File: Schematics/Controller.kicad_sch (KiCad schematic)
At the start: 25 parts, among them IC1 F280049CPMSR, J15 43650-0418, J19 FTSH-105-01-LM-D-K, J20 43650-0418, J22 43045-1212, Y1 ABM8-20.000MHZ-B2-T

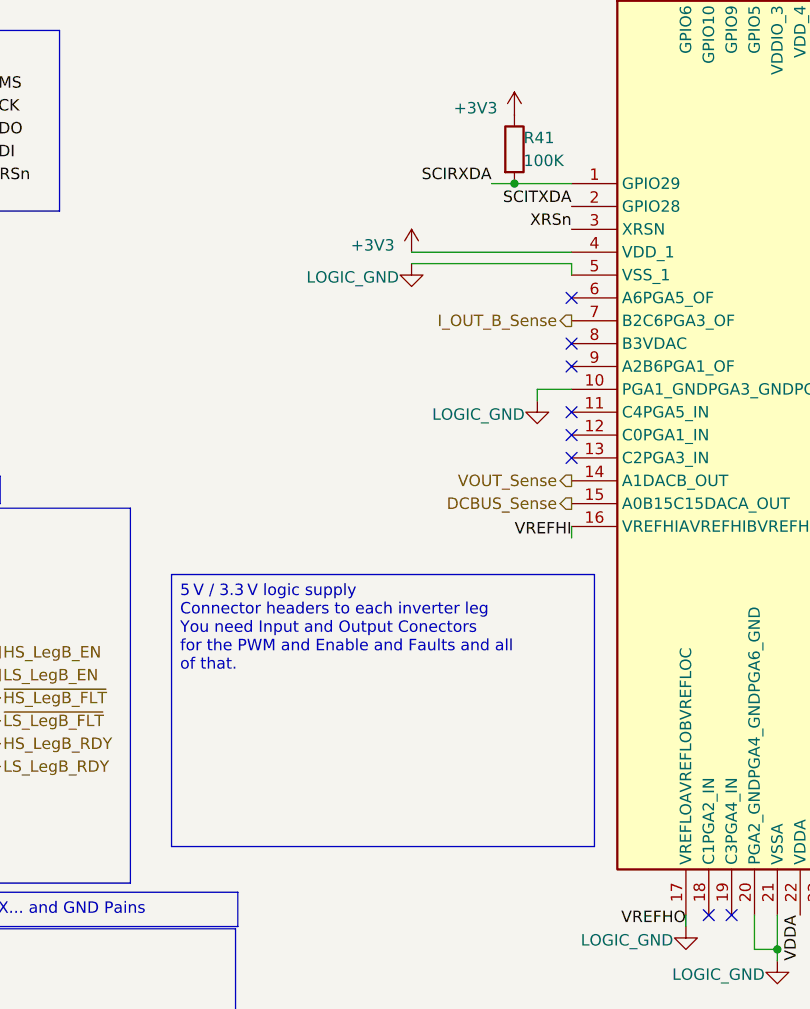
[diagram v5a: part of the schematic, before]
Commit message: [WIP Controller Subsheet]
- Added USB sub sheet to allow use of a USB connection to controller
- Added USB parts for USB Circuit
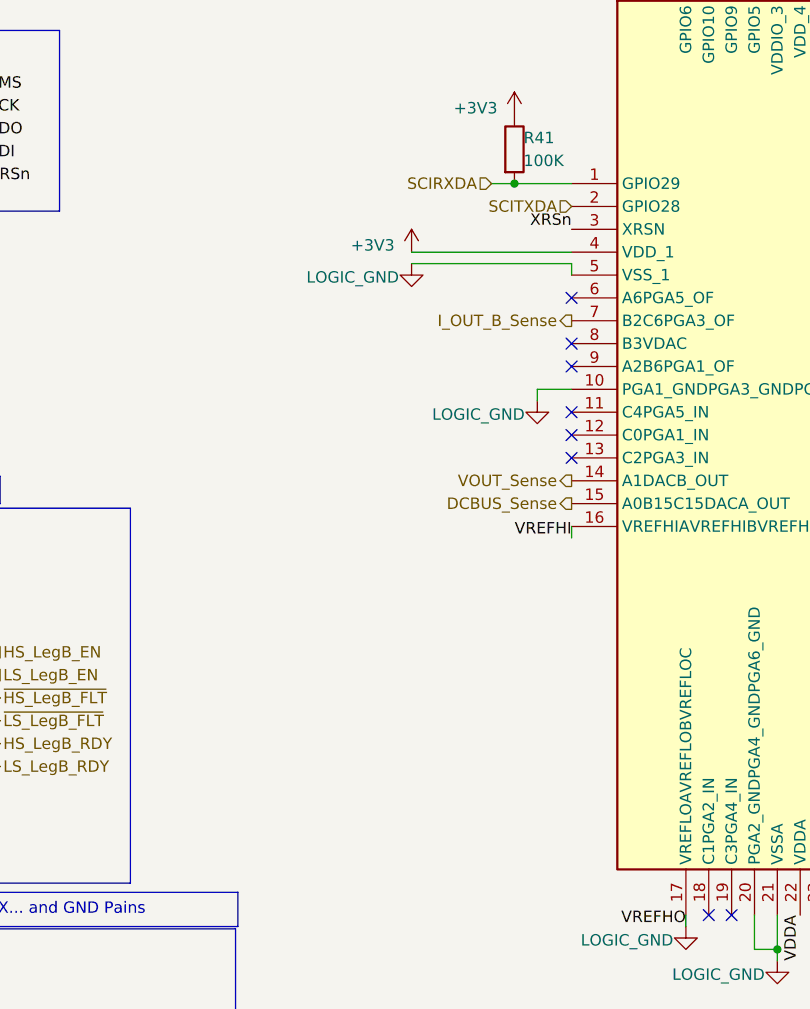
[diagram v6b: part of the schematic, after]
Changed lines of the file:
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@@
-		)
-	)
-	(text_box "5 V / 3.3 V logic supply\nConnector headers to each inverter leg\nYou need Input and Output Conectors \nfor the PWM and Enable and Faults and all of that. "
-		(exclude_from_sim no)
-		(at 73.66 108.204 0)
-		(size 46.99 30.226)
-		(margins 0.9525 0.9525 0.9525 0.9525)
-		(stroke
-			(width 0)
-			(type solid)
-		)
-		(fill
-			(type color)
-			(color 0 0 255 0.1)
-		)
-		(effects
-			(font
-				(size 1.27 1.27)
-			)
-			(justify left top)
 		)
 	)
@@
 		)
 	)
-	(label "SCITXDA"
-		(at 118.11 67.31 180)
-		(effects
-			(font
-				(size 1.27 1.27)
-			)
-			(justify right bottom)
-		)
-	)
 	(label "TCK"
 		(at 270.51 21.59 0)
@@
 			)
 			(justify left bottom)
-		)
-	)
-	(label "SCIRXDA"
-		(at 109.22 64.77 180)
-		(effects
-			(font
-				(size 1.27 1.27)
-			)
-			(justify right bottom)
 		)
 	)
@@
 		)
 	)
+	(hierarchical_label "SCIRXDA"
+		(shape input)
+		(at 109.22 64.77 180)
+		(effects
+			(font
+				(size 1.27 1.27)
+			)
+			(justify right)
+		)
+	)
 	(hierarchical_label "ePWM_A_H"
 		(shape input)
@@
 		(effects
 			(font
+				(size 1.27 1.27)
+			)
+			(justify right)
+		)
+	)
+	(hierarchical_label "SCITXDA"
+		(shape input)
+		(at 118.11 67.31 180)
+		(effects
+			(font

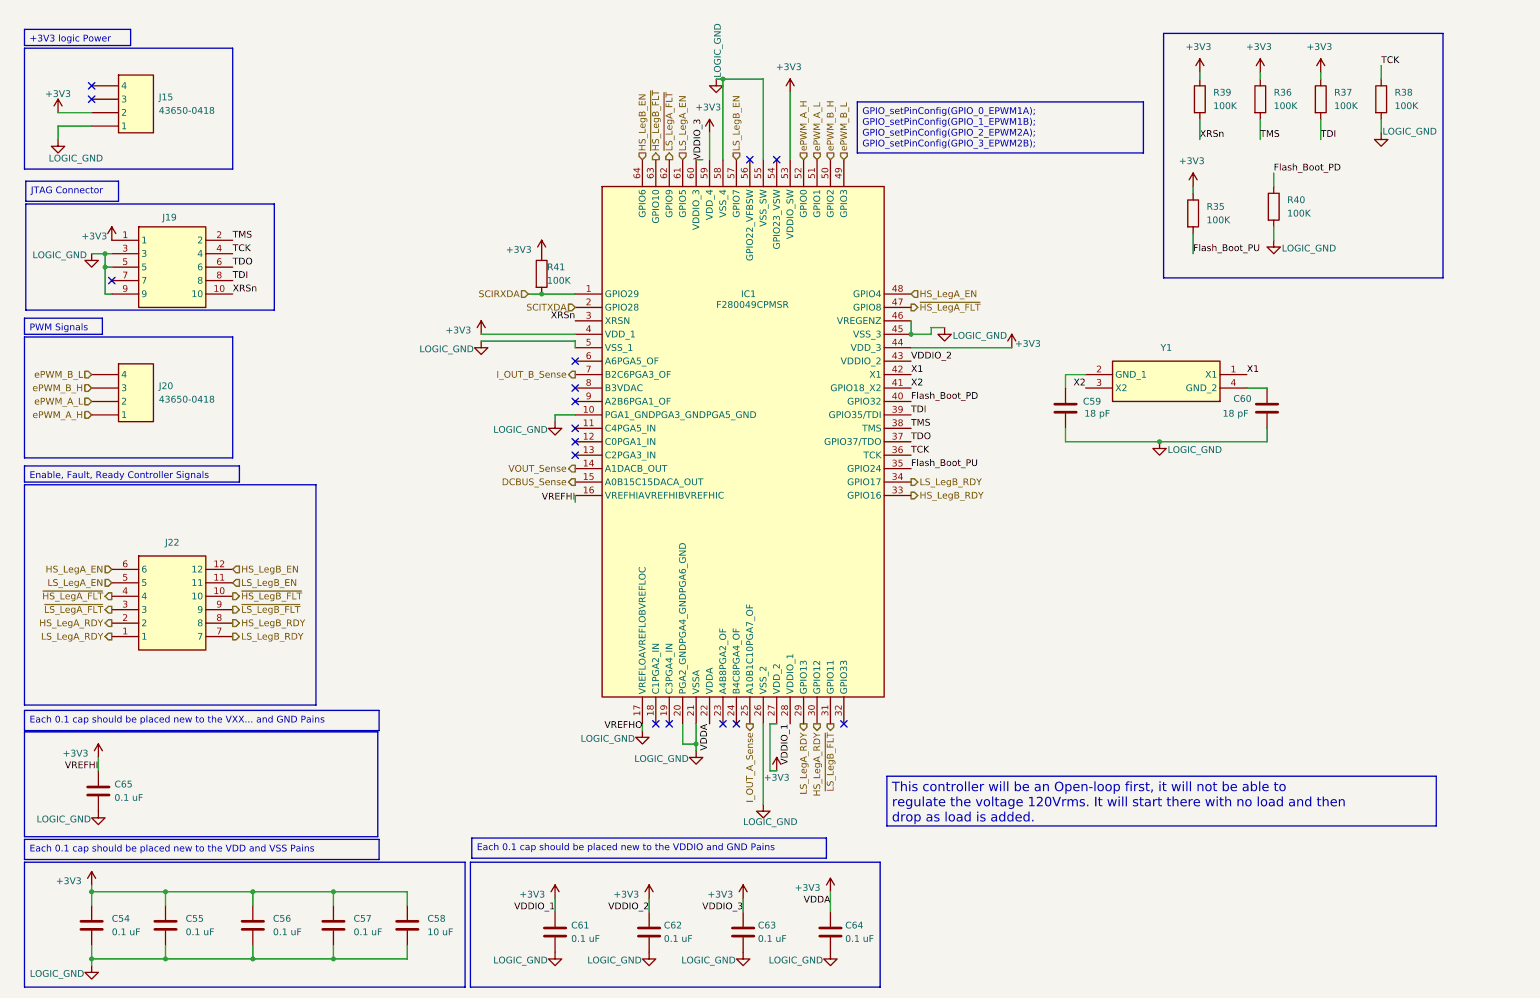
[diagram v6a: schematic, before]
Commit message: [Milestone Compelted Controller and USB]
- Added Test Points
- Completed USB circuit to Controller
- Wired up Controller
- Added Connectors to Power Subsheet and 12pin from cotnroller to Full
  Bridge
- Added 3d models for USB compoents
- General fixes to subsheets
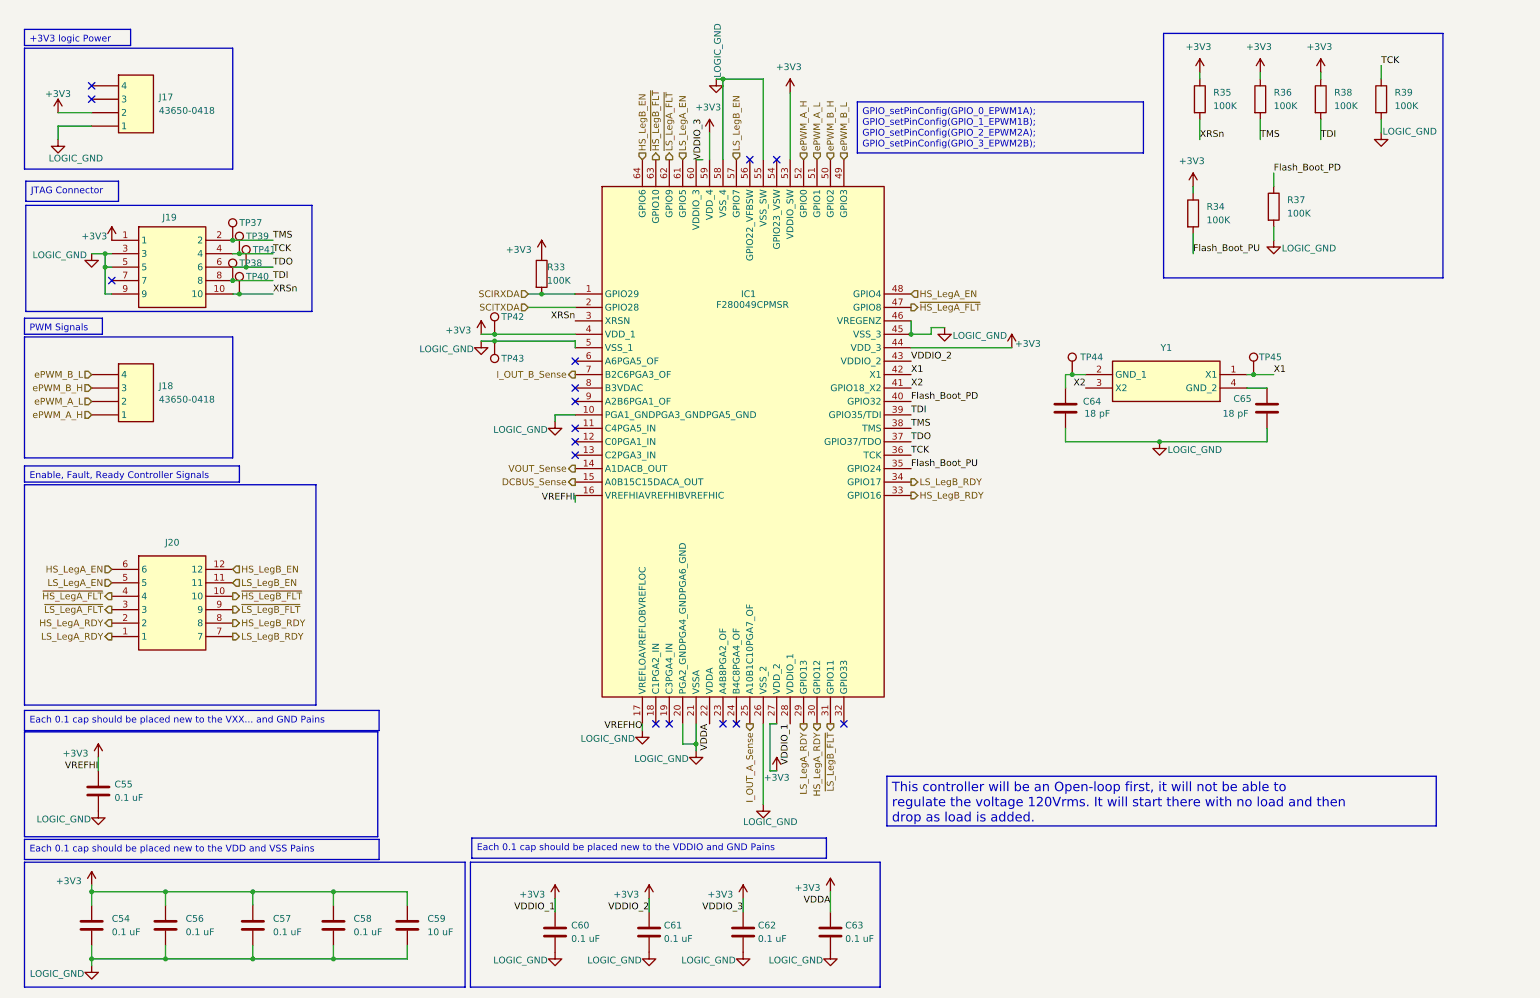
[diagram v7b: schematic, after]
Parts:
- added TP37, TP38, TP39, TP40, TP41, TP42, TP44: 5277, SiC_Inverter:5277, symbol SiC_Inverter:5277
- added TP43, TP45: 5281, SiC_Inverter:5281, symbol SiC_Inverter:5281
- renumbered C65 to C55, C55 to C56, C56 to C57, C57 to C58, C58 to C59, C61 to C60, C62 to C61, C63 to C62, C64 to C63, C59 to C64, C60 to C65, J15 to J17, J20 to J18, J22 to J20, R41 to R33, R35 to R34, R39 to R35, R40 to R37, R37 to R38, R38 to R39
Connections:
- net +3V3: now also TP42.1
- net LOGIC_GND: now also TP43.1
- net TCK: now also TP39.1
- net TDI: now also TP38.1
- net TDO: now also TP41.1
- net TMS: now also TP37.1
- net X1: now also TP45.1
- net XRSn: now also TP40.1
- net at C64.1, Y1.2 (GND_1): now also TP44.1

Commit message: [WIP Input Protection Circuit to Controller]
- Added Gate node input protection pin to controller
- Added optocoupler to input protection circuit
- Added 3d model for PC817.....
- Updated PCB to test out PCB modularity
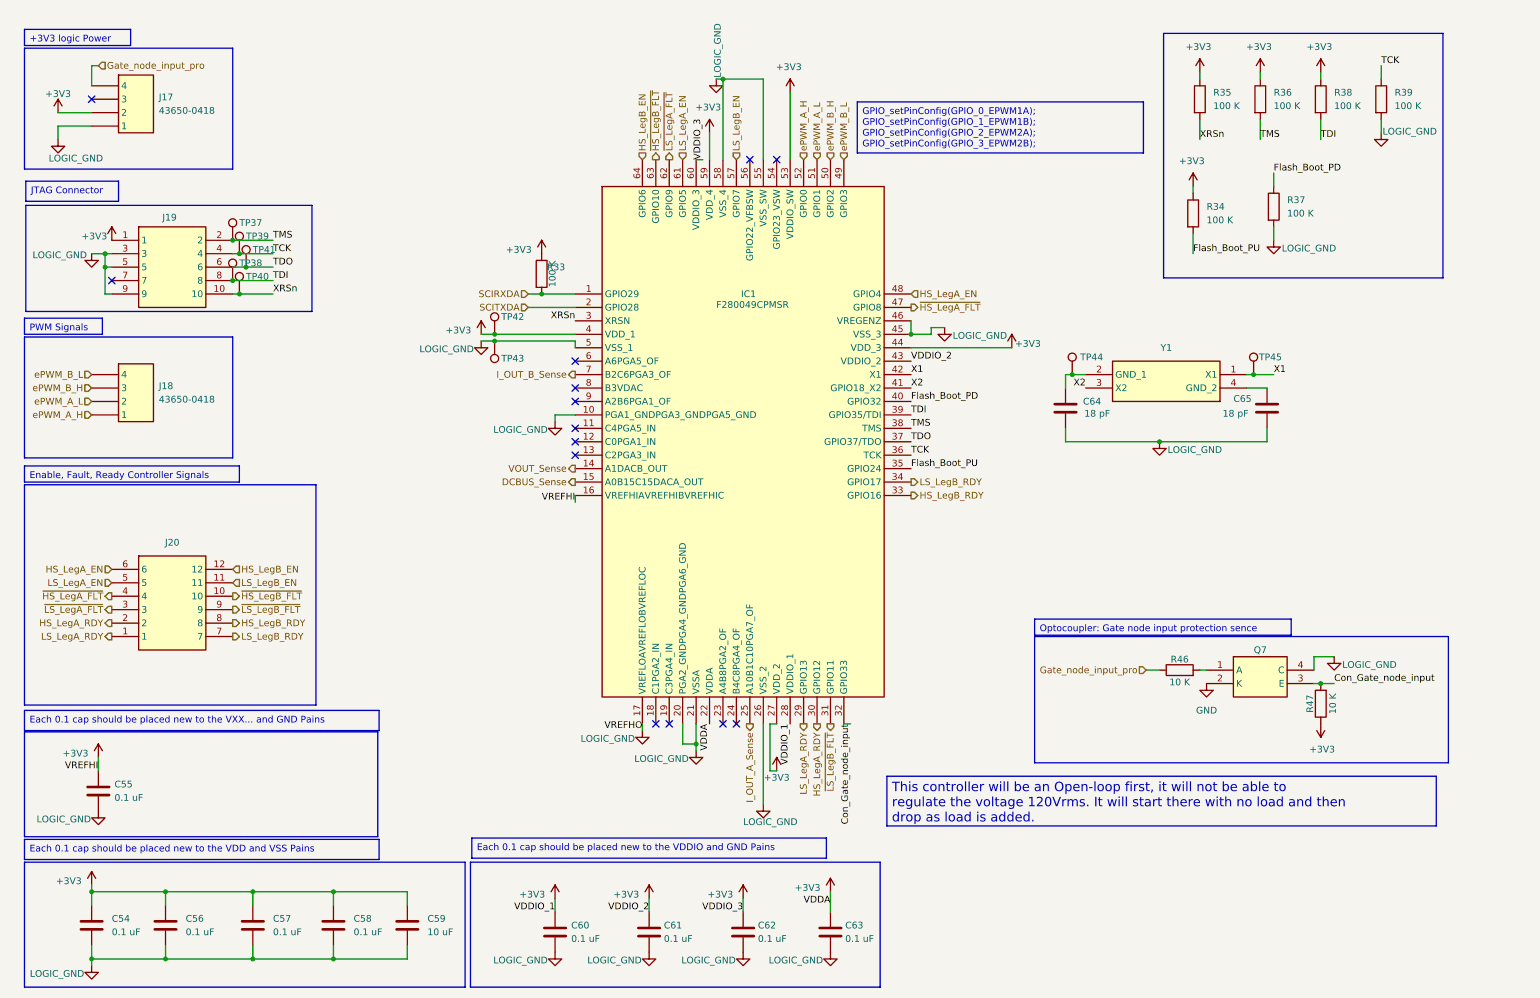
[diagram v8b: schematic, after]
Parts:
- added Q7: PC817X1CSP9F, SiC_Inverter:PC817X1CSP9F, symbol SiC_Inverter:PC817X1CSP9F
- added R46, R47: 10 K, Resistor_SMD:R_1206_3216Metric_Pad1.30x1.75mm_HandSolder, symbol SiC_Inverter:RT1206BRD0710KL
- R33, R34, R35, R36, R37, R38, R39: value 100K -> 100 K; symbol Device:R -> SiC_Inverter:RT1206BRD07100KL
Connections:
- net +3V3: now also R47.1
- net LOGIC_GND: now also Q7.4 (C)
- net Gate_node_input_pro: now reaches J17.4
- net Gate_node_input_pro: now also R46.1
- net Con_Gate_node_input: now reaches IC1.32 (GPIO33)
- net Con_Gate_node_input: now also Q7.3 (E), R47.2
- new net: Q7.1 (A), R46.2
- new net GND: Q7.2 (K)
- no-connect marks 16 -> 14
